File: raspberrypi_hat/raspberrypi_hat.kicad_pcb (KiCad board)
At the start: 4 copper layers, 65 x 56 mm, 18 parts, among them J3 40HAT, J6 CONN_02X02, J9 CONN_01X02, Q1 DMG2305UX, Q2 DMMT5401, U2 CAT24C32

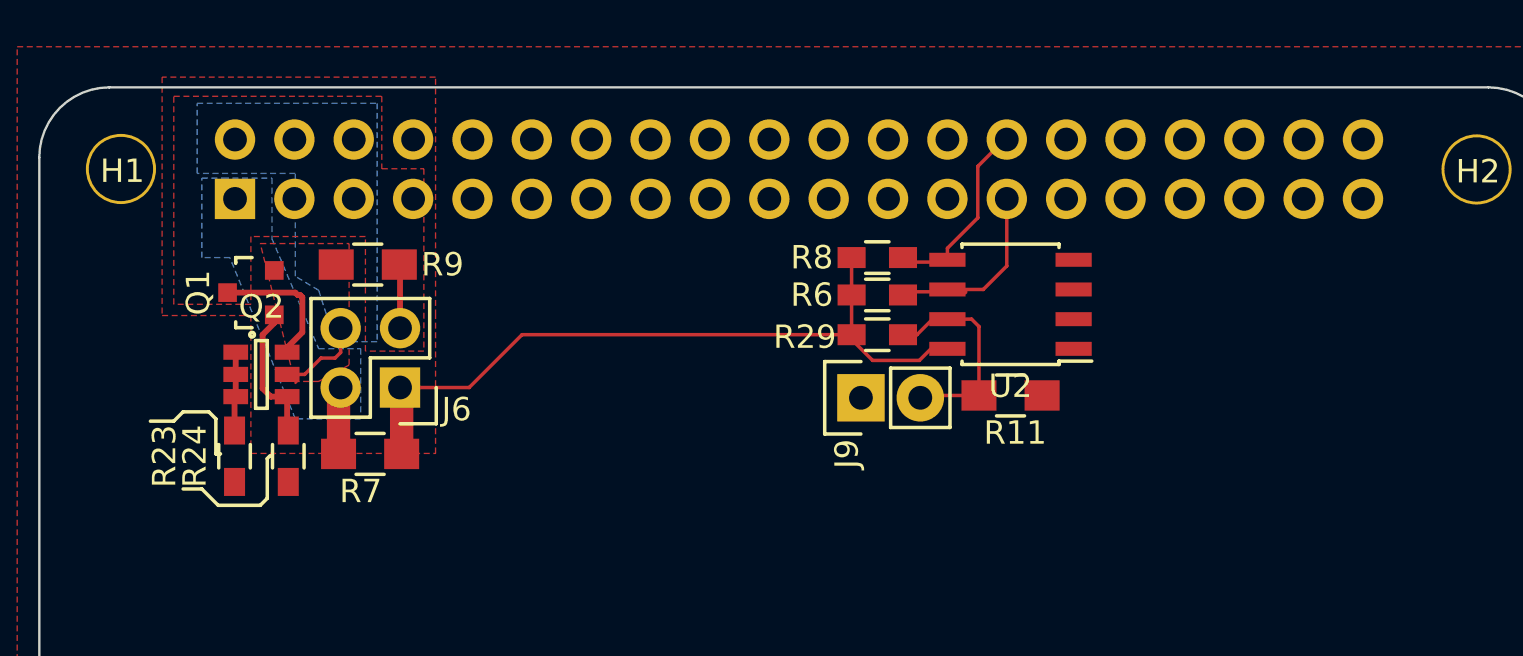
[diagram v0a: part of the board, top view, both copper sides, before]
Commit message: Update raspberrypi hat for new lib
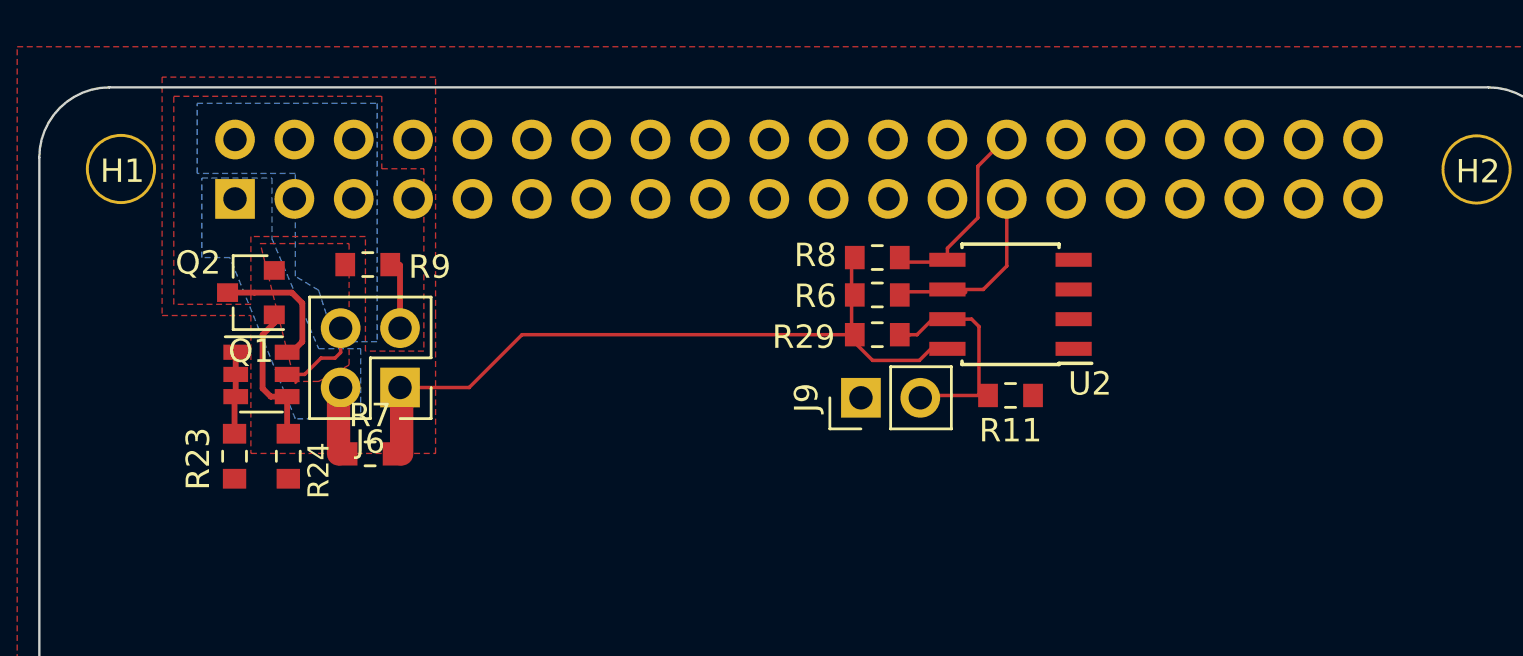
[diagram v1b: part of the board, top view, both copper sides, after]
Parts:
- J3: footprint Socket_Strips:Socket_Strip_Straight_2x20 -> Connector_PinSocket_2.54mm:PinSocket_2x20_P2.54mm_Vertical
- J6: footprint Pin_Headers:Pin_Header_Straight_2x02 -> Connector_PinHeader_2.54mm:PinHeader_2x02_P2.54mm_Vertical
- J9: footprint Pin_Headers:Pin_Header_Straight_1x02 -> Connector_PinHeader_2.54mm:PinHeader_1x02_P2.54mm_Vertical
- Q1: footprint TO_SOT_Packages_SMD:SOT-23 -> Package_TO_SOT_SMD:SOT-23
- Q2: footprint TO_SOT_Packages_SMD:SOT-23-6 -> Package_TO_SOT_SMD:SOT-23-6
- R11, R7, R9: footprint Resistors_SMD:R_0805_HandSoldering -> Resistor_SMD:R_0603_1608Metric_Pad0.84x1.00mm_HandSolder
- R23, R24, R29, R6, R8: footprint Resistors_SMD:R_0603_HandSoldering -> Resistor_SMD:R_0603_1608Metric_Pad0.84x1.00mm_HandSolder
- U2: footprint Housings_SOIC:SOIC-8_3.9x4.9mm_Pitch1.27mm -> Package_SOIC:SOIC-8_3.9x4.9mm_P1.27mm
- turned J3 to 270 degrees
- turned Q1 to 180 degrees
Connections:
- J3 pad 10: (no net) -> Net-(J3-Pad10)
- J3 pad 11: (no net) -> Net-(J3-Pad11)
- J3 pad 12: (no net) -> Net-(J3-Pad12)
- J3 pad 13: (no net) -> Net-(J3-Pad13)
- J3 pad 15: (no net) -> Net-(J3-Pad15)
- J3 pad 16: (no net) -> Net-(J3-Pad16)
- J3 pad 17: (no net) -> Net-(J3-Pad17)
- J3 pad 18: (no net) -> Net-(J3-Pad18)
- J3 pad 19: (no net) -> Net-(J3-Pad19)
- J3 pad 21: (no net) -> Net-(J3-Pad21)
- J3 pad 22: (no net) -> Net-(J3-Pad22)
- J3 pad 23: (no net) -> Net-(J3-Pad23)
- J3 pad 24: (no net) -> Net-(J3-Pad24)
- J3 pad 26: (no net) -> Net-(J3-Pad26)
- J3 pad 29: (no net) -> Net-(J3-Pad29)
- J3 pad 3: (no net) -> Net-(J3-Pad3)
- J3 pad 31: (no net) -> Net-(J3-Pad31)
- J3 pad 32: (no net) -> Net-(J3-Pad32)
- J3 pad 33: (no net) -> Net-(J3-Pad33)
- J3 pad 35: (no net) -> Net-(J3-Pad35)
- J3 pad 36: (no net) -> Net-(J3-Pad36)
- J3 pad 37: (no net) -> Net-(J3-Pad37)
- J3 pad 38: (no net) -> Net-(J3-Pad38)
- J3 pad 40: (no net) -> Net-(J3-Pad40)
- J3 pad 5: (no net) -> Net-(J3-Pad5)
- J3 pad 7: (no net) -> Net-(J3-Pad7)
- J3 pad 8: (no net) -> Net-(J3-Pad8)
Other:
- rule pad_to_mask_clearance: 0.2 -> 0.1
